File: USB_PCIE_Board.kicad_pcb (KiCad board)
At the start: 4 copper layers, 98.2 x 111.5 mm, 175 parts, among them J1 Bus_PCI_Express_x1, J2 0484050001, J3 0484050001, J4 0484050001, J5 0484050001, Q1 2SA1576AT106R, Q2 2SC4081T106R, Q4 DMT6016LSS-13, Q5 SI4134DY-T1-GE3, U1 UPD720201K8-711-BAC-A, U10 AP2191SG-13, U11 AP2191SG-13, U12 SP3011-06UTG, U13 SP3011-06UTG, U14 SP3011-06UTG, U15 SP3011-06UTG, U2 MX25L4006EM1I-12G, U3 LM22678TJ-5.0/NOPB, U4 LTC3872ETS8-TRPBF, U5 RT5762CHGH6F, U6 641737-1, U7 AP7215-33YG-13, U8 AP2191SG-13, U9 AP2191SG-13, X1 CS14522-24M

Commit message: Fix DRC errors: dangling vias, hole clearance, and courtyard issues
Address the bulk of the outstanding DRC violations flagged in the
design review, including dangling stitching vias and tight hole
clearances around U1's decoupling network.
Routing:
- net GND: vias 461 -> 458
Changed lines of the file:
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@@
 		(sheetname "/")
 		(sheetfile "USB_PCIE_Board.kicad_sch")
-		(units
-			(unit
-				(name "A")
-				(pins "1" "2" "3" "4" "5" "6" "7" "8" "9" "SH")
-			)
-		)
 		(attr through_hole)
 		(duplicate_pad_numbers_are_jumpers no)
@@
 		)
 		(fp_line
-			(start 11.25 12.82)
-			(end 10.9 12.82)
+			(start -3.9 12.82)
+			(end -3.9 4.09)
 			(stroke
 				(width 0.05)
@@
 		)
 		(fp_line
-			(start -3.9 12.8)
-			(end -3.9 4.09)
+			(start 11.25 12.82)
+			(end 10.9 12.82)
 			(stroke
 				(width 0.05)
@@
 		(fp_line
 			(start 10.9 4.09)
-			(end 10.9 12.8)
+			(end 10.9 12.82)
 			(stroke
 				(width 0.05)
@@
 		(sheetname "/")
 		(sheetfile "USB_PCIE_Board.kicad_sch")
-		(units
-			(unit
-				(name "A")
-				(pins "1" "2" "3" "4" "5" "6" "7" "8" "9" "SH")
-			)
-		)
 		(attr through_hole)
 		(duplicate_pad_numbers_are_jumpers no)
@@
 		)
 		(fp_line
-			(start 11.25 12.82)
-			(end 10.9 12.82)
+			(start -3.9 12.82)
+			(end -3.9 4.09)
 			(stroke
 				(width 0.05)
@@
 		)
 		(fp_line
-			(start -3.9 12.8)
-			(end -3.9 4.09)
+			(start 11.25 12.82)
+			(end 10.9 12.82)
 			(stroke
 				(width 0.05)
@@
 		(fp_line
 			(start 10.9 4.09)
-			(end 10.9 12.8)
+			(end 10.9 12.82)
 			(stroke
 				(width 0.05)
@@
 		(sheetname "/")
 		(sheetfile "USB_PCIE_Board.kicad_sch")
-		(units
-			(unit
-				(name "A")
-				(pins "1" "2" "3" "4" "5" "6" "7" "8" "9" "SH")
-			)
-		)
 		(attr through_hole)
 		(duplicate_pad_numbers_are_jumpers no)
@@
 		)
 		(fp_line
-			(start 11.25 12.82)
-			(end 10.9 12.82)
+			(start -3.9 12.82)
+			(end -3.9 4.09)
 			(stroke
 				(width 0.05)
@@
 		)
 		(fp_line
-			(start -3.9 12.8)
-			(end -3.9 4.09)
+			(start 11.25 12.82)
+			(end 10.9 12.82)
 			(stroke
 				(width 0.05)
@@
 		(fp_line
 			(start 10.9 4.09)
-			(end 10.9 12.8)
+			(end 10.9 12.82)
 			(stroke
 				(width 0.05)
@@
 		(sheetname "/")
 		(sheetfile "USB_PCIE_Board.kicad_sch")
-		(units
-			(unit
-				(name "A")
-				(pins "1" "2" "3" "4" "5" "6" "7" "8" "9" "SH")
-			)
-		)
 		(attr through_hole)
 		(duplicate_pad_numbers_are_jumpers no)
@@
 		)
 		(fp_line
-			(start 11.25 12.82)
-			(end 10.9 12.82)
+			(start -3.9 12.82)
+			(end -3.9 4.09)
 			(stroke
 				(width 0.05)
@@
 		)
 		(fp_line
-			(start -3.9 12.8)
-			(end -3.9 4.09)
+			(start 11.25 12.82)
+			(end 10.9 12.82)
 			(stroke
 				(width 0.05)
@@
 		(fp_line
 			(start 10.9 4.09)
-			(end 10.9 12.8)
+			(end 10.9 12.82)
 			(stroke
 				(width 0.05)
@@
 	)
 	(via
-		(at 122 41.75)
+		(at 122 41.65)
 		(size 0.35)
 		(drill 0.2)
@@
 	)
 	(via
-		(at 112.1 39.3)
+		(at 112.1 39.6)
 		(size 0.35)
 		(drill 0.2)
@@
 	)
 	(via
-		(at 102 39.4)
+		(at 102 39.6)
 		(size 0.35)
 		(drill 0.2)
@@
 	)
 	(via
-		(at 88.1 39.55)
+		(at 88.1 39.6)
 		(size 0.35)
 		(drill 0.2)
@@
 	)
 	(via
-		(at 120 41.8)
+		(at 120 41.65)
 		(size 0.35)
 		(drill 0.2)
@@
 	)
 	(via
-		(at 84.1 39.5)
+		(at 84.1 39.6)
 		(size 0.35)
 		(drill 0.2)
@@
 	)
 	(via
-		(at 133.55 127.7)
-		(size 0.35)
-		(drill 0.2)
-		(layers "F.Cu" "B.Cu")
-		(free yes)
-		(net "GND")
-	)
-	(via
-		(at 82.1 39.5)
+		(at 82.1 39.6)
 		(size 0.35)
 		(drill 0.2)
@@
 	)
 	(via
-		(at 78.1 39.55)
+		(at 78.1 39.6)
 		(size 0.35)
 		(drill 0.2)
@@
 	)
 	(via
-		(at 131.9 39.4)
+		(at 131.9 39.6)
 		(size 0.35)
 		(drill 0.2)
@@
 	)
 	(via
-		(at 133.8 39.4)
+		(at 133.8 39.6)
 		(size 0.35)
 		(drill 0.2)
@@
 	)
 	(via
-		(at 124 39.5)
+		(at 124 39.6)
 		(size 0.35)
 		(drill 0.2)
@@
 	)
 	(via
-		(at 127.9 39.45)
+		(at 127.9 39.6)
 		(size 0.35)
 		(drill 0.2)
@@
 	)
 	(via
-		(at 86 39.5)
+		(at 86 39.6)
 		(size 0.35)
 		(drill 0.2)
@@
 	)
 	(via
-		(at 122 39.5)
+		(at 122 39.6)
 		(size 0.35)
 		(drill 0.2)
@@
 	)
 	(via
-		(at 133.5 41.7)
+		(at 133.5 41.65)
 		(size 0.35)
 		(drill 0.2)
@@
 	)
 	(via
-		(at 100 39.4)
+		(at 100 39.6)
 		(size 0.35)
 		(drill 0.2)
@@
 	)
 	(via
-		(at 103.9 39.4)
+		(at 103.9 39.6)
 		(size 0.35)
 		(drill 0.2)
@@
 	)
 	(via
-		(at 67.8 39.8)
+		(at 67.8 39.6)
 		(size 0.6)
 		(drill 0.3)
@@
 	)
 	(via
-		(at 80.1 39.55)
+		(at 80.1 39.6)
 		(size 0.35)
 		(drill 0.2)
@@
 	)
 	(via
-		(at 124 41.75)
+		(at 124 41.65)
 		(size 0.35)
 		(drill 0.2)
@@
 	)
 	(via
-		(at 65.5 39.8)
+		(at 65.5 39.6)
 		(size 0.6)
 		(drill 0.3)
@@
 	)
 	(via
-		(at 133.55 129.6)
-		(size 0.35)
-		(drill 0.2)
-		(layers "F.Cu" "B.Cu")
-		(free yes)
-		(net "GND")
-	)
-	(via
 		(at 95.983765 105.274603)
 		(size 0.35)
@@
 	)
 	(via
-		(at 129.9 39.4)
+		(at 129.9 39.6)
 		(size 0.35)
 		(drill 0.2)
@@
 	)
 	(via
-		(at 118.1 39.35)
+		(at 118.1 39.6)
 		(size 0.35)
 		(drill 0.2)
@@
 	)
 	(via
-		(at 70 39.65)
+		(at 70 39.6)
 		(size 0.35)
 		(drill 0.2)
@@
 	)
 	(via
-		(at 96 39.5)
+		(at 96 39.6)
 		(size 0.35)
 		(drill 0.2)
@@
 	)
 	(via
-		(at 90.1 39.55)
+		(at 90.1 39.6)
 		(size 0.35)
 		(drill 0.2)
@@
 	)
 	(via
-		(at 97.65 90.7)
+		(at 97.8 90.8)
 		(size 0.35)
 		(drill 0.2)
@@
 	)
 	(via
-		(at 106.1 39.35)
+		(at 106.1 39.6)
 		(size 0.35)
 		(drill 0.2)
@@
 	)
 	(via
-		(at 108.1 39.35)
+		(at 108.1 39.6)
 		(size 0.35)
 		(drill 0.2)
@@
 	)
 	(via
-		(at 125.9 41.75)
+		(at 125.9 41.65)
 		(size 0.35)
 		(drill 0.2)
@@
 	)
 	(via
-		(at 98 39.45)
+		(at 98 39.6)
 		(size 0.35)
 		(drill 0.2)
@@
 	)
 	(via
-		(at 114 39.3)
+		(at 114 39.6)
 		(size 0.35)
 		(drill 0.2)
@@
 	)
 	(via
-		(at 116.1 39.35)
+		(at 116.1 39.6)
 		(size 0.35)
 		(drill 0.2)
@@
 	)
 	(via
-		(at 110.1 39.3)
+		(at 110.1 39.6)
 		(size 0.35)
 		(drill 0.2)
@@
 	)
 	(via
-		(at 120 39.55)
+		(at 120 39.6)
 		(size 0.35)
 		(drill 0.2)
@@
 	)
 	(via
-		(at 125.9 39.5)
+		(at 125.9 39.6)
 		(size 0.35)
 		(drill 0.2)
@@
 	)
 	(via
-		(at 133.55 125.7)
-		(size 0.35)
-		(drill 0.2)
-		(layers "F.Cu" "B.Cu")
-		(free yes)
-		(net "GND")
-	)
-	(via
 		(at 132.8 70.25)
 		(size 0.35)
@@
 	)
 	(via
-		(at 92.1 39.5)
+		(at 92.1 39.6)
 		(size 0.35)
 		(drill 0.2)
@@
 	)
 	(via
-		(at 94.1 39.5)
+		(at 94.1 39.6)
 		(size 0.35)
 		(drill 0.2)
@@
 			)
 		)
+	)
+	(zone
+		(net "GND")
+		(layer "B.Cu")
+		(hatch none 0.5)
+		(priority 92)
+		(connect_pads yes
+			(clearance 0.75)
+		)
+		(min_thickness 0.25)
+		(fill yes
+			(thermal_gap 0.5)
+			(thermal_bridge_width 0.5)
+			(island_removal_mode 0)
+		)
+		(polygon
+			(pts
+				(xy 62.8 38.2) (xy 149.6 38.2) (xy 149.6 137) (xy 119.4 137) (xy 119.4 132.6) (xy 90.8 132.6) (xy 90.8 137)
+				(xy 62.8 137)
+			)
+		)

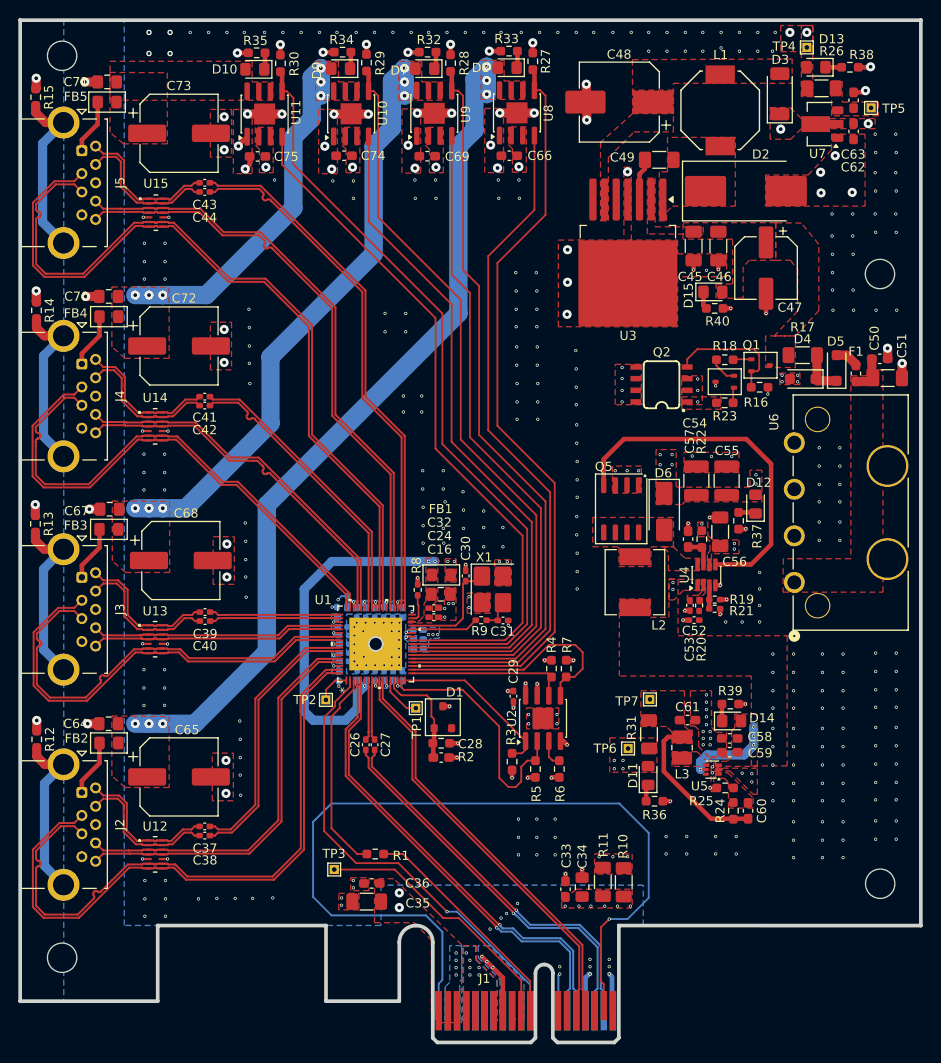
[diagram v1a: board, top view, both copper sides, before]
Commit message: Move PCIe diff-pair decoupling caps closer per host chip guidance; add fab tables to drawing layer
Relocate the capacitors on the PCIe differential pair closer to the
card edge per the host chip manufacturer's layout guidance, and add
stackup/fabrication info tables to the drawing layer. Regenerate
fabrication outputs (gerbers, drill files, netlist, BOM) to match.
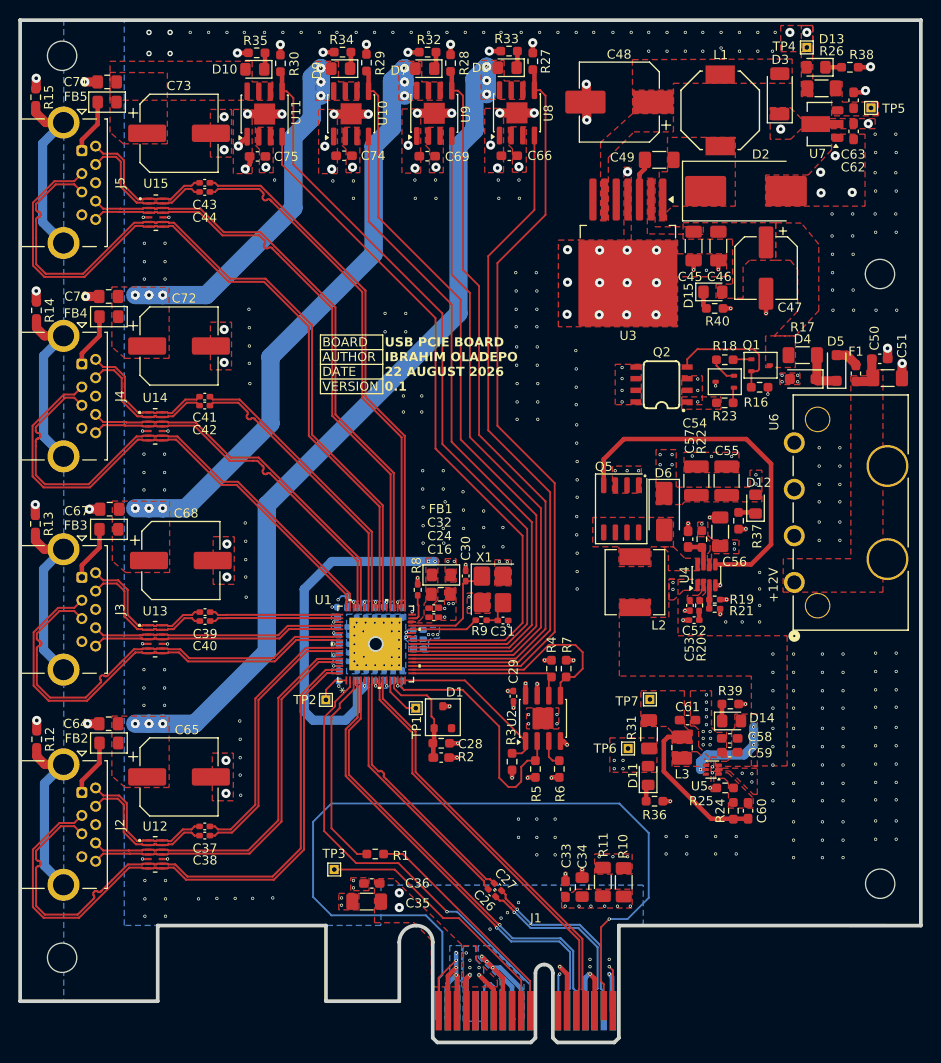
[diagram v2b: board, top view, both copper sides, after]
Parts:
- D10, D7, D8, D9: value LED_0805_WHITE -> LED_WH
- D11, D12, D13: value LED_0805_BLUE -> LED_BL
- D14, D15: value LED_0805_YELLOW -> LED_YE
- moved C26 21.2 mm to (102.9, 133.4), turned to 135 degrees
- moved C27 20.5 mm to (103.5, 132.8), turned to -45 degrees
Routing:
- net GND: track 83.0 -> 110.0 mm, vias 458 -> 466
- net +3V3_INT: track 33.4 -> 59.6 mm
- net +12V: track 0.00 -> 25.9 mm
- net PETXP: track 42.3 -> 20.5 mm
- net PETX_HP: track 6.59 -> 28.2 mm
- net PETX_HN: track 6.59 -> 28.2 mm
- net PETXN: track 42.3 -> 20.8 mm
- net Net-(J1-JTAG3): track 0.00 -> 6.65 mm
- net Net-(C52-Pad2): track 0.00 -> 1.01 mm
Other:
- board text added: "+12V"
- board text added: "BOARD AUTHOR DATE VERSION"
- board text added: "COMPONENT TYPES"
- board text added: "DRILL TABLE"
- board text added: "LAYER STACKUP [4 LAYERS]"
- board text added: "REMARKS"
- board text added: "USB PCIE BOARD IBRAHIM OLADEPO 22 AUGUST 2026 0.1"
- board text added: "• Total Board Thickness: 1.6062mm • Finish: ENIG • Impedance Controlled: Yes • Plated Edges: Yes • Edge Connector: Yes • Minimum Trace Width/Space: 0.2mm/0.2mm • Minimum Via Size: Hole Diameter 0.2mm / Round Diameter 0.35 mm • Impedance Control: - USB: 90Ω-Differential, Trace Width 0.2187mm (8.61mil) / Spacing 0.127mm (5.0mil) - PCIE: 90Ω-Differential, Trace Width 0.2187mm (8.61mil) / Spacing 0.1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"
